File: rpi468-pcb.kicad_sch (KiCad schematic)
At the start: 11 parts, among them J1 USB_A, J2 USB_C_Receptacle_USB2.0, J3 Conn_01x04_Female, U1 LM397

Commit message: layingout the board again
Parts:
- J2: footprint Connector_USB:USB_C_Receptacle_Amphenol_12401548E4-2A -> Connector_USB:USB_C_Receptacle_Amphenol_12401610E4-2A
- R1, R2, R3, R4, R5, R6: footprint Resistor_SMD:R_0805_2012Metric -> Resistor_SMD:R_0603_1608Metric_Pad0.98x0.95mm_HandSolder
- S1: renamed from S?; footprint (none) -> Package_DFN_QFN:DFN-10-1EP_3x3mm_P0.5mm_EP1.75x2.7mm
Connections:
- net at J2.B5 (CC2), R2.1: now also U1.1 (-)
- net at J2.A5 (CC1), R1.1: no longer U1.1 (-)
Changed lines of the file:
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@@
 (kicad_sch (version 20211123) (generator eeschema)
   (paper "A4")
-  (junction (at 100.33 86.36) (diameter 0) (color 0 0 0 0)
-  )
   (junction (at 80.01 62.23) (diameter 0) (color 0 0 0 0)
   )
   (junction (at 100.33 96.52) (diameter 0) (color 0 0 0 0)
+  )
+  (junction (at 100.33 88.9) (diameter 0) (color 0 0 0 0)
   )
   (junction (at 193.04 100.33) (diameter 0) (color 0 0 0 0)
@@
     (stroke (width 0) (type default) (color 0 0 0 0))
   )
-  (wire (pts (xy 100.33 83.82) (xy 110.49 83.82))
-    (stroke (width 0) (type default) (color 0 0 0 0))
-  )
   (wire (pts (xy 125.73 140.97) (xy 140.97 140.97))
     (stroke (width 0) (type default) (color 0 0 0 0))
@@
     (stroke (width 0) (type default) (color 0 0 0 0))
   )
-  (wire (pts (xy 180.34 58.42) (xy 180.34 93.98))
-    (stroke (width 0) (type default) (color 0 0 0 0))
-  )
   (wire (pts (xy 100.33 96.52) (xy 124.46 96.52))
     (stroke (width 0) (type default) (color 0 0 0 0))
@@
     (stroke (width 0) (type default) (color 0 0 0 0))
   )
+  (wire (pts (xy 100.33 92.71) (xy 121.92 92.71))
+    (stroke (width 0) (type default) (color 0 0 0 0))
+  )
   (wire (pts (xy 157.48 96.52) (xy 157.48 125.73))
     (stroke (width 0) (type default) (color 0 0 0 0))
@@
     (stroke (width 0) (type default) (color 0 0 0 0))
   )
+  (wire (pts (xy 121.92 92.71) (xy 121.92 105.41))
+    (stroke (width 0) (type default) (color 0 0 0 0))
+  )
   (wire (pts (xy 129.54 54.61) (xy 129.54 85.09))
     (stroke (width 0) (type default) (color 0 0 0 0))
@@
     (stroke (width 0) (type default) (color 0 0 0 0))
   )
-  (wire (pts (xy 110.49 58.42) (xy 180.34 58.42))
-    (stroke (width 0) (type default) (color 0 0 0 0))
-  )
   (wire (pts (xy 193.04 82.55) (xy 193.04 80.01))
     (stroke (width 0) (type default) (color 0 0 0 0))
@@
     (stroke (width 0) (type default) (color 0 0 0 0))
   )
-  (wire (pts (xy 110.49 58.42) (xy 110.49 83.82))
-    (stroke (width 0) (type default) (color 0 0 0 0))
-  )
   (wire (pts (xy 229.87 87.63) (xy 219.71 87.63))
     (stroke (width 0) (type default) (color 0 0 0 0))
@@
     (stroke (width 0) (type default) (color 0 0 0 0))
   )
+  (wire (pts (xy 100.33 88.9) (xy 100.33 92.71))
+    (stroke (width 0) (type default) (color 0 0 0 0))
+  )
   (wire (pts (xy 123.19 104.14) (xy 163.83 104.14))
     (stroke (width 0) (type default) (color 0 0 0 0))
@@
     (stroke (width 0) (type default) (color 0 0 0 0))
   )
+  (wire (pts (xy 121.92 105.41) (xy 180.34 105.41))
+    (stroke (width 0) (type default) (color 0 0 0 0))
+  )
   (wire (pts (xy 157.48 92.71) (xy 161.29 92.71))
     (stroke (width 0) (type default) (color 0 0 0 0))
@@
     (stroke (width 0) (type default) (color 0 0 0 0))
   )
-  (wire (pts (xy 100.33 86.36) (xy 100.33 83.82))
+  (wire (pts (xy 180.34 105.41) (xy 180.34 93.98))
     (stroke (width 0) (type default) (color 0 0 0 0))
   )
@@
       (effects (font (size 1.27 1.27)) (justify left))
     )
-    (property "Footprint" "Resistor_SMD:R_0805_2012Metric" (id 2) (at 191.262 104.14 90)
+    (property "Footprint" "Resistor_SMD:R_0603_1608Metric_Pad0.98x0.95mm_HandSolder" (id 2) (at 191.262 104.14 90)
       (effects (font (size 1.27 1.27)) hide)
     )
@@
     (property "Reference" "R2" (id 0) (at 104.14 88.9 90))
     (property "Value" "5.1k" (id 1) (at 104.14 91.44 90))
-    (property "Footprint" "Resistor_SMD:R_0805_2012Metric" (id 2) (at 104.14 90.678 90)
+    (property "Footprint" "Resistor_SMD:R_0603_1608Metric_Pad0.98x0.95mm_HandSolder" (id 2) (at 104.14 90.678 90)
       (effects (font (size 1.27 1.27)) hide)
     )
@@
     (property "Reference" "R6" (id 0) (at 214.63 77.47 90))
     (property "Value" "5.1k" (id 1) (at 214.63 82.55 90))
-    (property "Footprint" "Resistor_SMD:R_0805_2012Metric" (id 2) (at 214.63 81.788 90)
+    (property "Footprint" "Resistor_SMD:R_0603_1608Metric_Pad0.98x0.95mm_HandSolder" (id 2) (at 214.63 81.788 90)
       (effects (font (size 1.27 1.27)) hide)
     )
@@
       (effects (font (size 1.27 1.27)) (justify left))
     )
-    (property "Footprint" "Resistor_SMD:R_0805_2012Metric" (id 2) (at 191.262 86.36 90)
+    (property "Footprint" "Resistor_SMD:R_0603_1608Metric_Pad0.98x0.95mm_HandSolder" (id 2) (at 191.262 86.36 90)
       (effects (font (size 1.27 1.27)) hide)
     )
@@
   (symbol (lib_id "library:ISL54225") (at 146.05 81.28 0) (unit 1)
     (in_bom yes) (on_board yes)
-    (property "Reference" "S?" (id 0) (at 146.05 74.93 0))
+    (property "Reference" "S1" (id 0) (at 146.05 74.93 0))
     (property "Value" "ISL54225" (id 1) (at 146.05 77.47 0))
-    (property "Footprint" "" (id 2) (at 146.05 81.28 0)
+    (property "Footprint" "Package_DFN_QFN:DFN-10-1EP_3x3mm_P0.5mm_EP1.75x2.7mm" (id 2) (at 146.05 81.28 0)
       (effects (font (size 1.27 1.27)) hide)
     )
@@
     (property "Reference" "J2" (id 0) (at 85.09 73.66 0))
     (property "Value" "USB_C_Receptacle_USB2.0" (id 1) (at 85.09 76.2 0))
-    (property "Footprint" "Connector_USB:USB_C_Receptacle_Amphenol_12401548E4-2A" (id 2) (at 88.9 96.52 0)
+    (property "Footprint" "Connector_USB:USB_C_Receptacle_Amphenol_12401610E4-2A" (id 2) (at 88.9 96.52 0)
       (effects (font (size 1.27 1.27)) hide)
     )
@@
     (property "Reference" "R5" (id 0) (at 209.55 97.79 90))
     (property "Value" "50k" (id 1) (at 209.55 102.87 90))
-    (property "Footprint" "Resistor_SMD:R_0805_2012Metric" (id 2) (at 209.55 102.108 90)
+    (property "Footprint" "Resistor_SMD:R_0603_1608Metric_Pad0.98x0.95mm_HandSolder" (id 2) (at 209.55 102.108 90)
       (effects (font (size 1.27 1.27)) hide)
     )
@@
     (property "Reference" "R1" (id 0) (at 104.14 86.36 90))
     (property "Value" "5.1k" (id 1) (at 104.14 83.82 90))
-    (property "Footprint" "Resistor_SMD:R_0805_2012Metric" (id 2) (at 104.14 88.138 90)
+    (property "Footprint" "Resistor_SMD:R_0603_1608Metric_Pad0.98x0.95mm_HandSolder" (id 2) (at 104.14 88.138 90)
       (effects (font (size 1.27 1.27)) hide)
     )
@@
     )
     (path "/bc32768b-85e6-4895-85d8-acf87f438080"
-      (reference "J2") (unit 1) (value "USB_C_Receptacle_USB2.0") (footprint "Connector_USB:USB_C_Receptacle_Amphenol_12401548E4-2A")
+      (reference "J2") (unit 1) (value "USB_C_Receptacle_USB2.0") (footprint "Connector_USB:USB_C_Receptacle_Amphenol_12401610E4-2A")
     )
     (path "/e68b378b-715b-4790-8da2-8ea2e44dd6a6"
@@
     )
     (path "/f619ccc9-65b6-46d1-9876-505c58d8035a"
-      (reference "R1") (unit 1) (value "5.1k") (footprint "Resistor_SMD:R_0805_2012Metric")
+      (reference "R1") (unit 1) (value "5.1k") (footprint "Resistor_SMD:R_0603_1608Metric_Pad0.98x0.95mm_HandSolder")
     )
     (path "/2fa03c2b-51fc-4456-bdb0-f263cbb97ec2"
-      (reference "R2") (unit 1) (value "5.1k") (footprint "Resistor_SMD:R_0805_2012Metric")
+      (reference "R2") (unit 1) (value "5.1k") (footprint "Resistor_SMD:R_0603_1608Metric_Pad0.98x0.95mm_HandSolder")
     )
     (path "/6da03d20-475c-43ba-9c2d-1d8574e4fab1"
-      (reference "R3") (unit 1) (value "100k") (footprint "Resistor_SMD:R_0805_2012Metric")
+      (reference "R3") (unit 1) (value "100k") (footprint "Resistor_SMD:R_0603_1608Metric_Pad0.98x0.95mm_HandSolder")
     )
     (path "/1829c383-9c86-4d52-a146-f19816fab1a7"
-      (reference "R4") (unit 1) (value "1k") (footprint "Resistor_SMD:R_0805_2012Metric")
+      (reference "R4") (unit 1) (value "1k") (footprint "Resistor_SMD:R_0603_1608Metric_Pad0.98x0.95mm_HandSolder")
     )
     (path "/de324e25-0d21-4c49-8736-7d79013e10c4"
-      (reference "R5") (unit 1) (value "50k") (footprint "Resistor_SMD:R_0805_2012Metric")
+      (reference "R5") (unit 1) (value "50k") (footprint "Resistor_SMD:R_0603_1608Metric_Pad0.98x0.95mm_HandSolder")
     )
     (path "/38762778-9a44-491f-be9d-282c618545cb"
-      (reference "R6") (unit 1) (value "5.1k") (footprint "Resistor_SMD:R_0805_2012Metric")
+      (reference "R6") (unit 1) (value "5.1k") (footprint "Resistor_SMD:R_0603_1608Metric_Pad0.98x0.95mm_HandSolder")
     )
     (path "/79c45e63-ba55-4398-a9ee-f0bf60391ac7"
-      (reference "S?") (unit 1) (value "ISL54225") (footprint "")
+      (reference "S1") (unit 1) (value "ISL54225") (footprint "Package_DFN_QFN:DFN-10-1EP_3x3mm_P0.5mm_EP1.75x2.7mm")
     )
     (path "/f911c51f-a1bc-45ca-acf5-2820d357c16a"

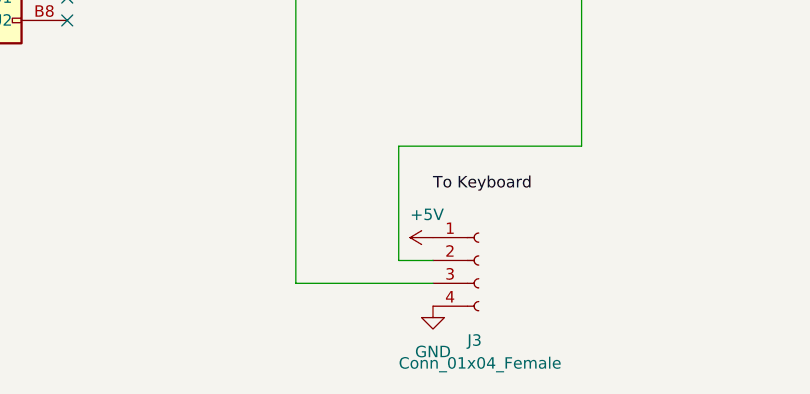
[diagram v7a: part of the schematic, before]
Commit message: updated board for 1mm pitch connector, reran some traces
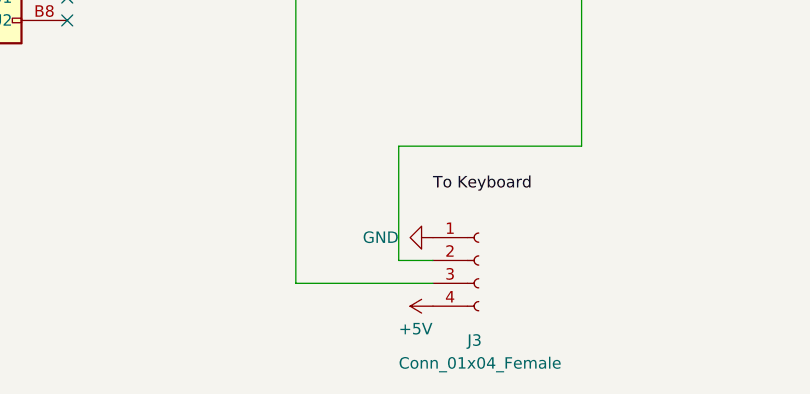
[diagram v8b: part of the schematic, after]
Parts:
- J3: footprint Connector_Wuerth:Wuerth_WR-WTB_64800411622_1x04_P1.50mm_Vertical -> Connector_PinHeader_1.00mm:PinHeader_1x04_P1.00mm_Vertical
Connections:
- net +5V: now also J3.4 (Pin_4); no longer J3.1 (Pin_1)
- net GND: now also J3.1 (Pin_1); no longer J3.4 (Pin_4)
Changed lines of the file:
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@@
     (pin "2")
   )
-  (symbol (lib_id "power:+5V") (at 140.97 135.89 90) (unit 1)
-    (in_bom yes) (on_board yes)
-    (property "Reference" "#PWR08" (id 0) (at 144.78 135.89 0)
-      (effects (font (size 1.27 1.27)) hide)
-    )
-    (property "Value" "+5V" (id 1) (at 138.43 133.35 90)
-      (effects (font (size 1.27 1.27)) (justify right))
-    )
-    (property "Footprint" "" (id 2) (at 140.97 135.89 0)
-      (effects (font (size 1.27 1.27)) hide)
-    )
-    (property "Datasheet" "" (id 3) (at 140.97 135.89 0)
+  (symbol (lib_id "power:+5V") (at 140.97 143.51 90) (unit 1)
+    (in_bom yes) (on_board yes)
+    (property "Reference" "#PWR08" (id 0) (at 144.78 143.51 0)
+      (effects (font (size 1.27 1.27)) hide)
+    )
+    (property "Value" "+5V" (id 1) (at 137.16 146.05 90)
+      (effects (font (size 1.27 1.27)) (justify right))
+    )
+    (property "Footprint" "" (id 2) (at 140.97 143.51 0)
+      (effects (font (size 1.27 1.27)) hide)
+    )
+    (property "Datasheet" "" (id 3) (at 140.97 143.51 0)
       (effects (font (size 1.27 1.27)) hide)
     )
@@
     (pin "S1")
   )
-  (symbol (lib_id "power:GND") (at 140.97 143.51 0) (unit 1)
-    (in_bom yes) (on_board yes) (fields_autoplaced)
-    (property "Reference" "#PWR09" (id 0) (at 140.97 149.86 0)
-      (effects (font (size 1.27 1.27)) hide)
-    )
-    (property "Value" "GND" (id 1) (at 140.97 148.59 0))
-    (property "Footprint" "" (id 2) (at 140.97 143.51 0)
-      (effects (font (size 1.27 1.27)) hide)
-    )
-    (property "Datasheet" "" (id 3) (at 140.97 143.51 0)
+  (symbol (lib_id "power:GND") (at 140.97 135.89 270) (unit 1)
+    (in_bom yes) (on_board yes) (fields_autoplaced)
+    (property "Reference" "#PWR09" (id 0) (at 134.62 135.89 0)
+      (effects (font (size 1.27 1.27)) hide)
+    )
+    (property "Value" "GND" (id 1) (at 137.16 135.8899 90)
+      (effects (font (size 1.27 1.27)) (justify right))
+    )
+    (property "Footprint" "" (id 2) (at 140.97 135.89 0)
+      (effects (font (size 1.27 1.27)) hide)
+    )
+    (property "Datasheet" "" (id 3) (at 140.97 135.89 0)
       (effects (font (size 1.27 1.27)) hide)
     )
@@
       (effects (font (size 1.27 1.27)) (justify left))
     )
-    (property "Footprint" "Connector_Wuerth:Wuerth_WR-WTB_64800411622_1x04_P1.50mm_Vertical" (id 2) (at 146.05 138.43 0)
+    (property "Footprint" "Connector_PinHeader_1.00mm:PinHeader_1x04_P1.00mm_Vertical" (id 2) (at 146.05 138.43 0)
       (effects (font (size 1.27 1.27)) hide)
     )
@@
     )
     (path "/e68b378b-715b-4790-8da2-8ea2e44dd6a6"
-      (reference "J3") (unit 1) (value "Conn_01x04_Female") (footprint "Connector_Wuerth:Wuerth_WR-WTB_64800411622_1x04_P1.50mm_Vertical")
+      (reference "J3") (unit 1) (value "Conn_01x04_Female") (footprint "Connector_PinHeader_1.00mm:PinHeader_1x04_P1.00mm_Vertical")
     )
     (path "/f619ccc9-65b6-46d1-9876-505c58d8035a"
